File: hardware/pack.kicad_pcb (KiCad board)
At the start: 2 copper layers, 96 x 90 mm, 124 parts, among them U1 MT3608

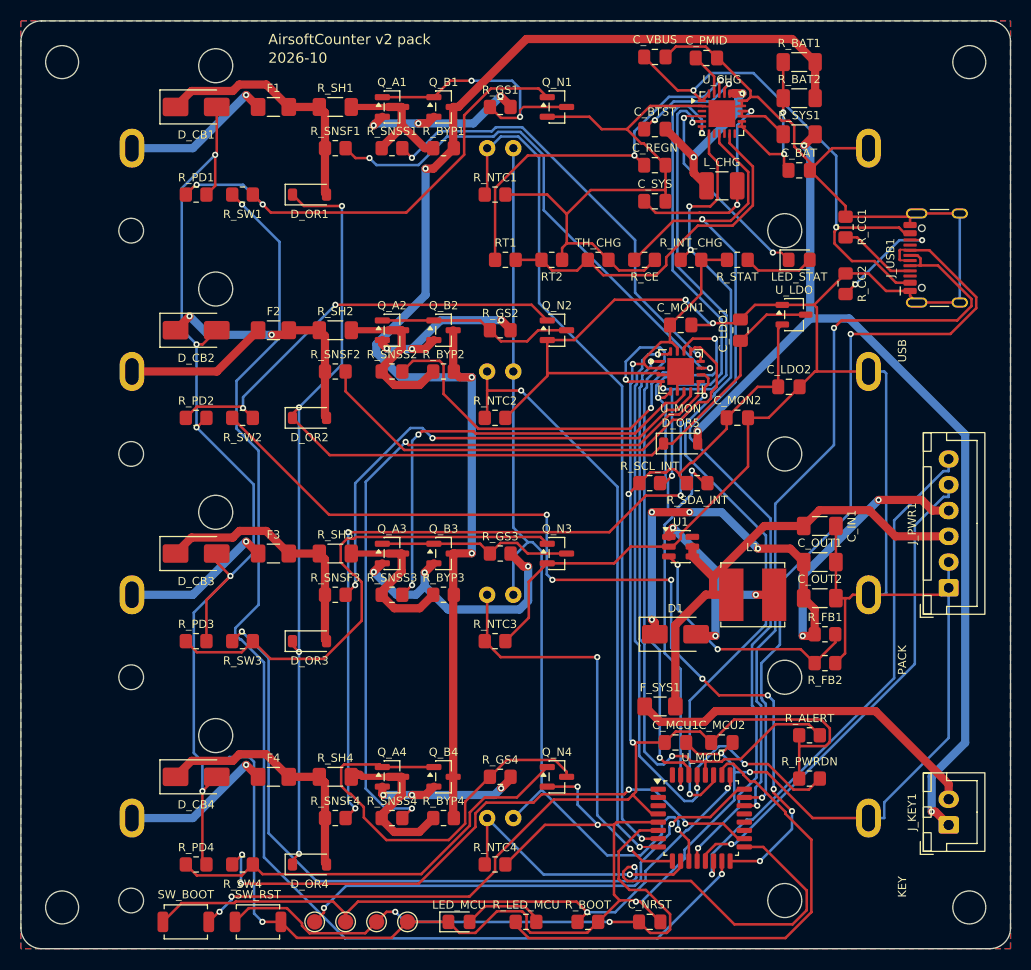
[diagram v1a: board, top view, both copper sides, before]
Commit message: hw: re-route the pack board with today's generators
The committed routing predates a later generator/KiCad change: rebuilding gives the same
placement, nets and JLC BOM/CPL but different Freerouting copper (1158 segments / 152 vias,
was 1246 / 148). Rebuilds are deterministic again, so the cleanup can diff against HEAD.
DRC clean, check_gerbers ok.

Co-Authored-By: Claude Opus 5.5 <noreply@anthropic.com>
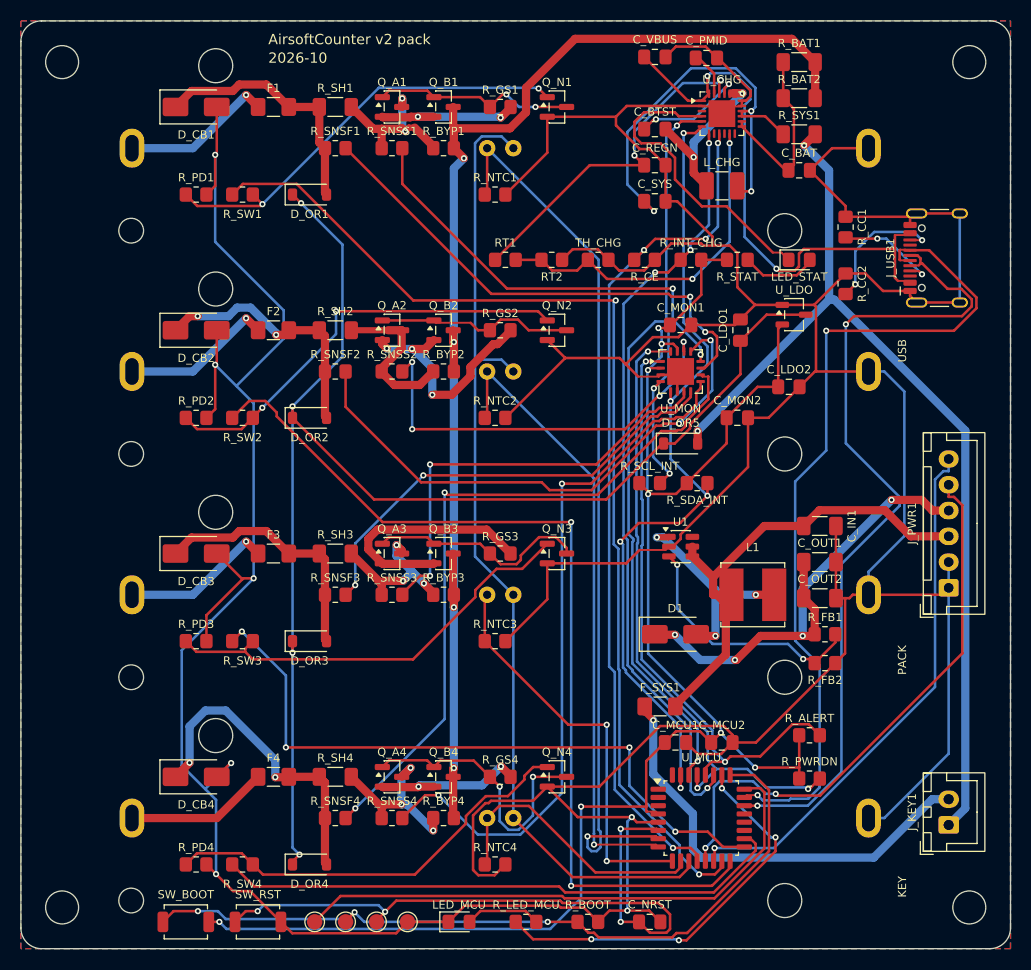
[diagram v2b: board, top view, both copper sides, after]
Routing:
- net SW3_DRV: track 92.6 -> 65.0 mm, vias 2 -> 4
- net SW1_DRV: track 122.5 -> 104.6 mm
- net SYS_CHG: track 27.5 -> 43.8 mm, vias 2 -> 3
- net CELL4_G: track 41.1 -> 27.7 mm, vias 0 -> 2
- net +5V: track 60.8 -> 47.7 mm, vias 6 -> 4
- net SCL_INT: track 102.3 -> 89.8 mm, vias 5 -> 4
- net LED_MCU_DRV: track 50.3 -> 39.3 mm, vias 0 -> 4
- net BOOT0: track 66.2 -> 75.9 mm, vias 2 -> 3
- net CHG_CE: track 93.4 -> 83.7 mm, vias 2 -> 4
- net STAT: track 20.3 -> 29.6 mm, vias 2 -> 0
- net SDA_INT: track 90.6 -> 81.2 mm, vias 4 -> 5
- net KEY_OUT: track 34.9 -> 43.3 mm, vias 0 -> 1
- net SDA_EXT: track 47.7 -> 55.3 mm, vias 1 -> 2
- net CHG_INT: track 81.5 -> 74.2 mm, vias 3 -> 4
- net SNS_F4: track 75.5 -> 68.3 mm, vias 4 -> 2
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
